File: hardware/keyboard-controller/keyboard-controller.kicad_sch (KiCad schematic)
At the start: 35 parts, among them J1 Debug_Pins, SW1 MODE_SEL, SW2 SUB_MODE, SW3 CLK_DIV, U2 Pico, U3 MCP4921

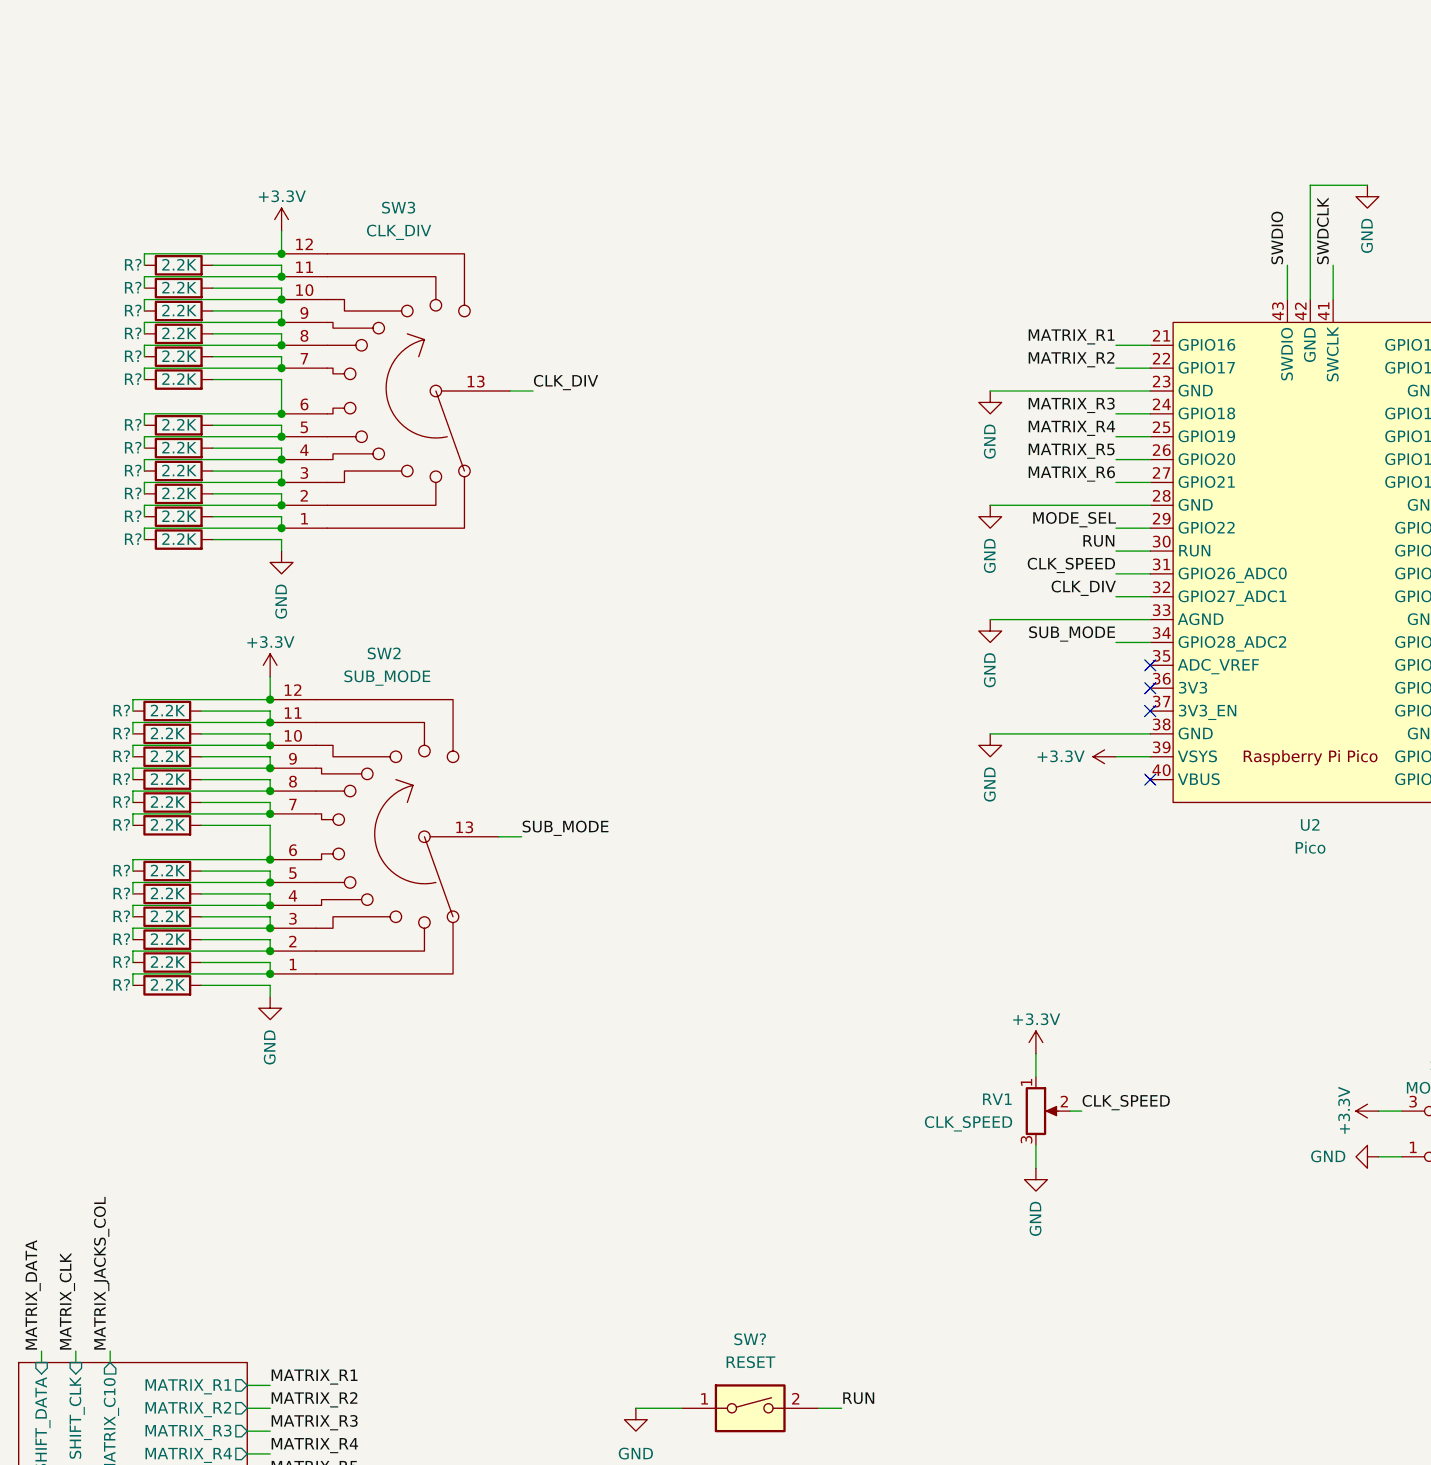
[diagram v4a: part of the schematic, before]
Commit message: Added filter caps on pots and rotary switches
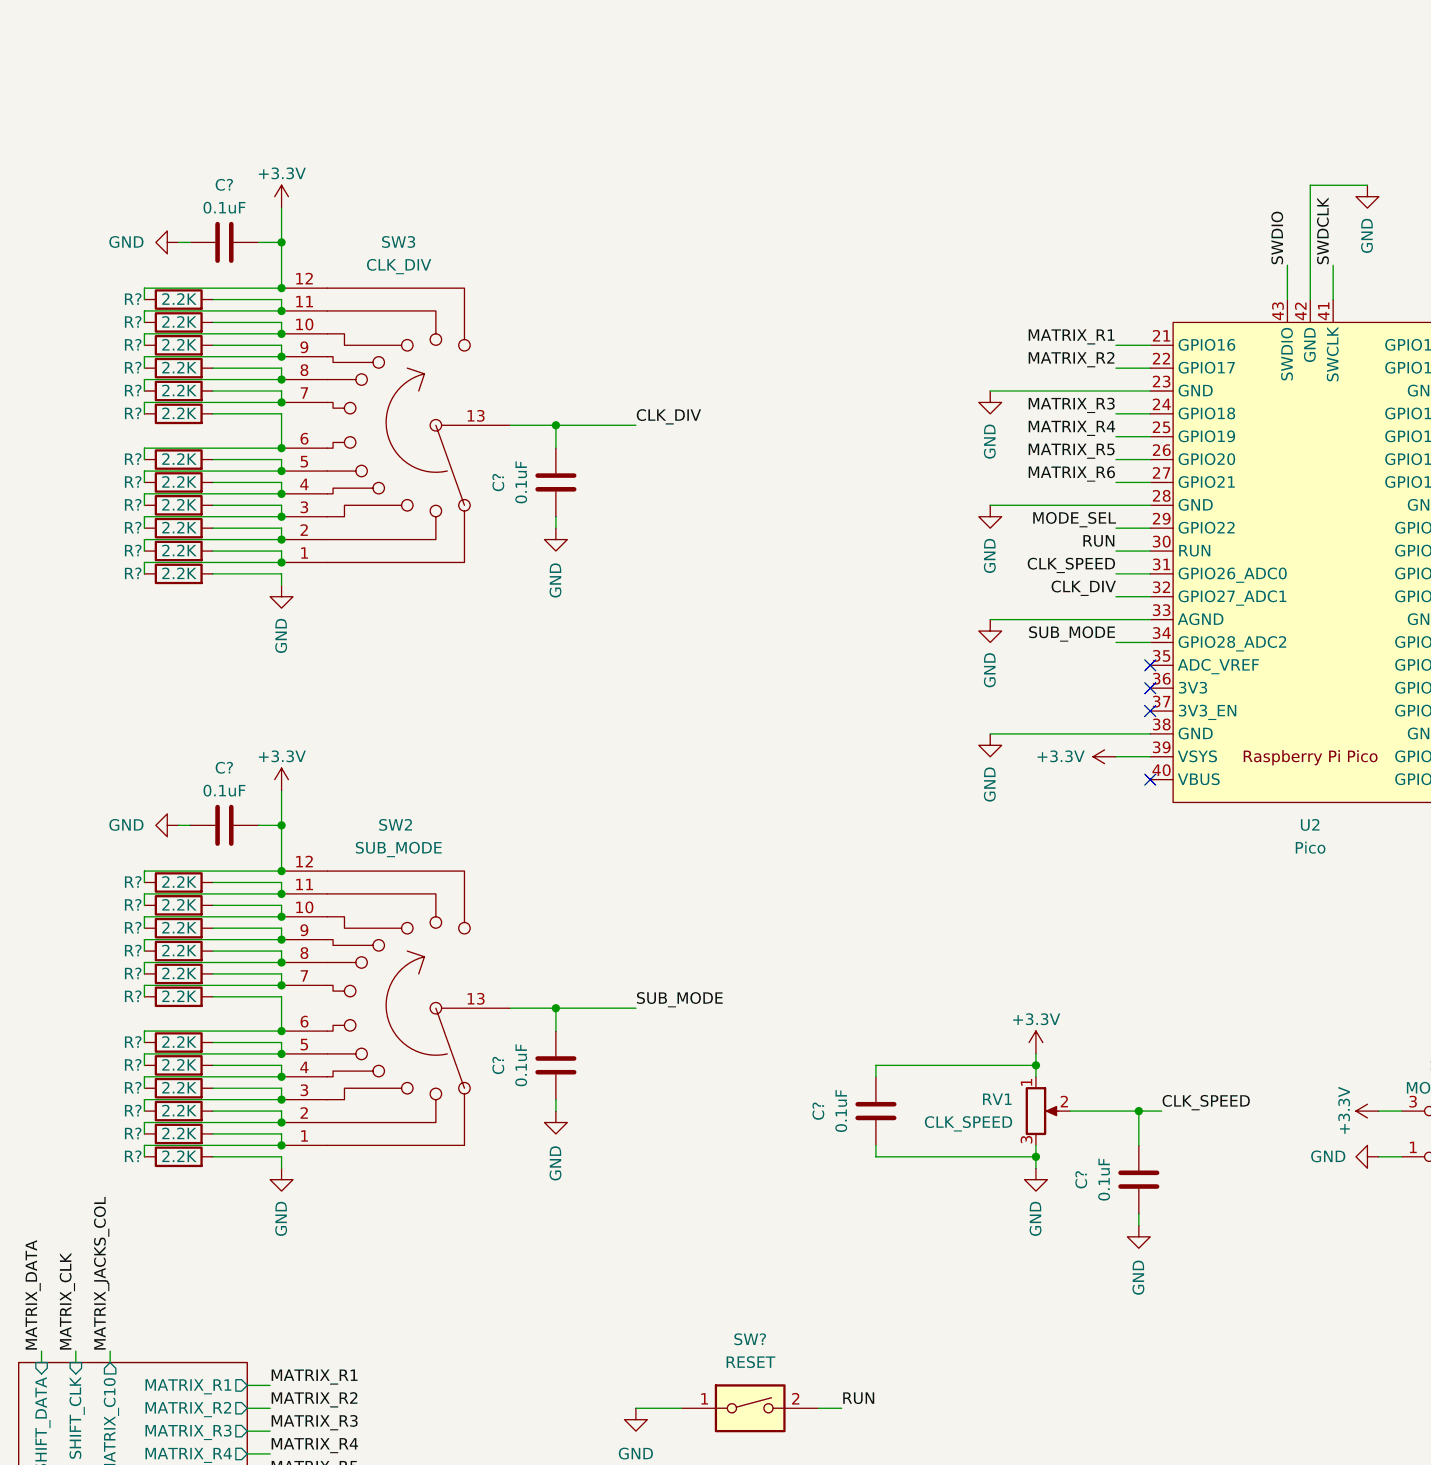
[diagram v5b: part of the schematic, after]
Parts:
- added C? (x6): 0.1uF, AEC_Capacitors:C_Disc_D5.0mm_W2.5mm_P3.0mm, symbol Device:C
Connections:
- net +3V3: now also C?.2, C?.2, C?.2
- net CLK_DIV: now also C?.2
- net CLK_SPEED: now also C?.2
- net GND: now also C?.1, C?.1, C?.1, C?.1, C?.1, C?.1
- net SUB_MODE: now also C?.2
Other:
- moved on the sheet: R?, SW2, SW3

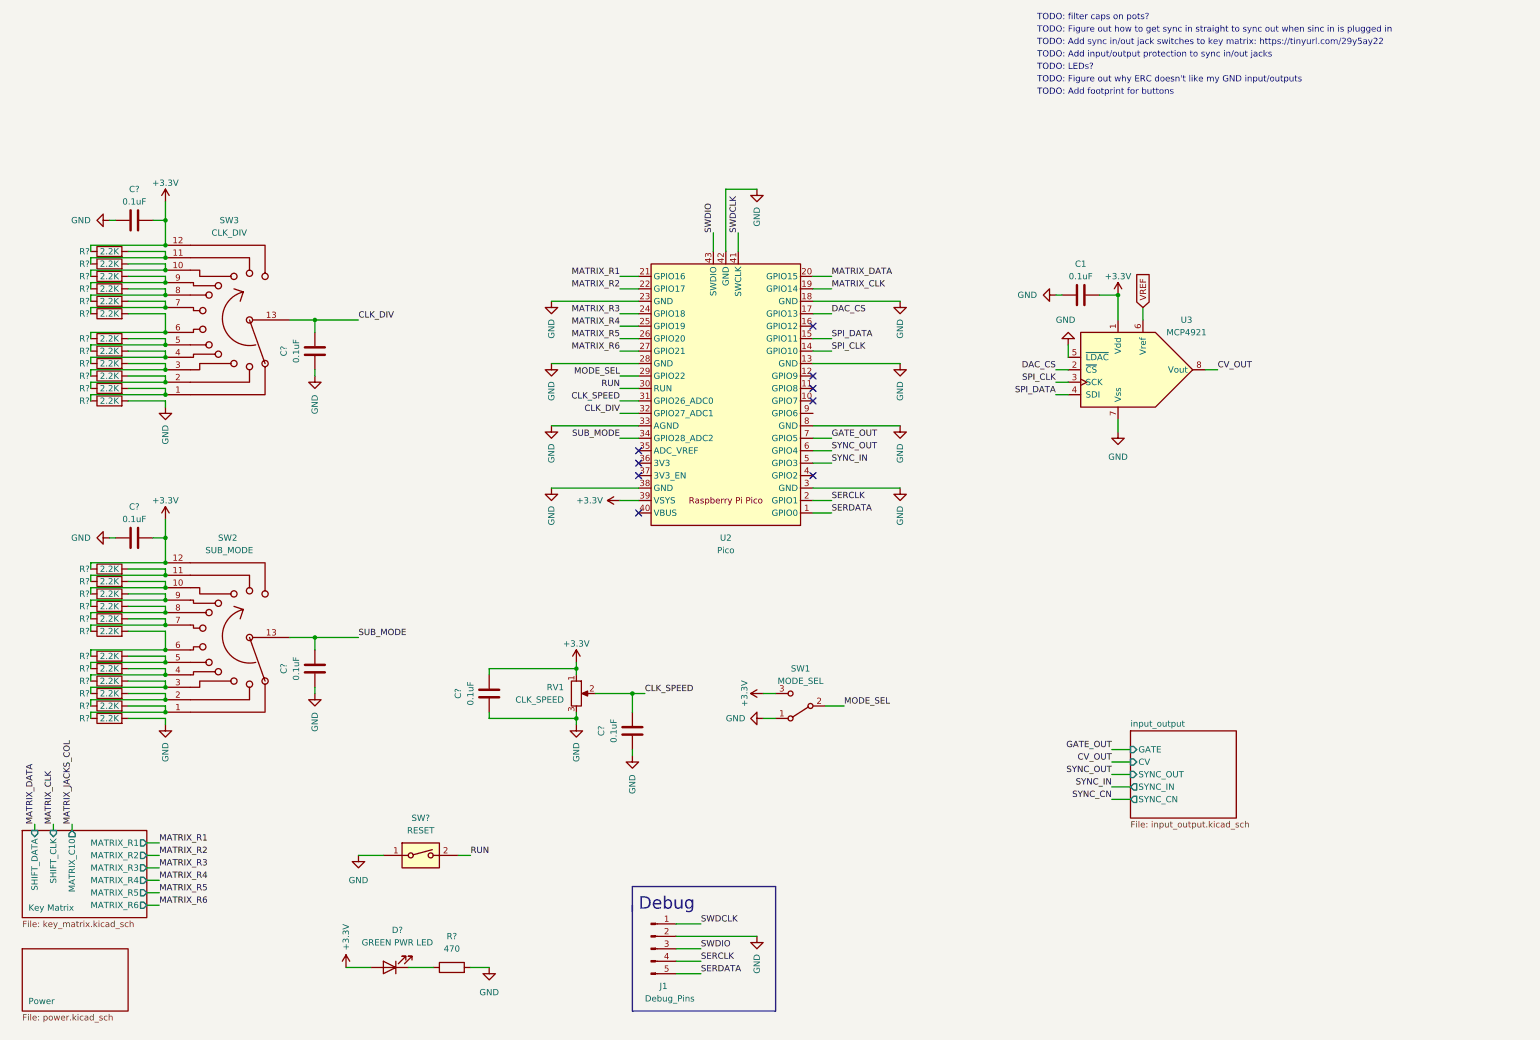
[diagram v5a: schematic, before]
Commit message: Added analog switch for analog input
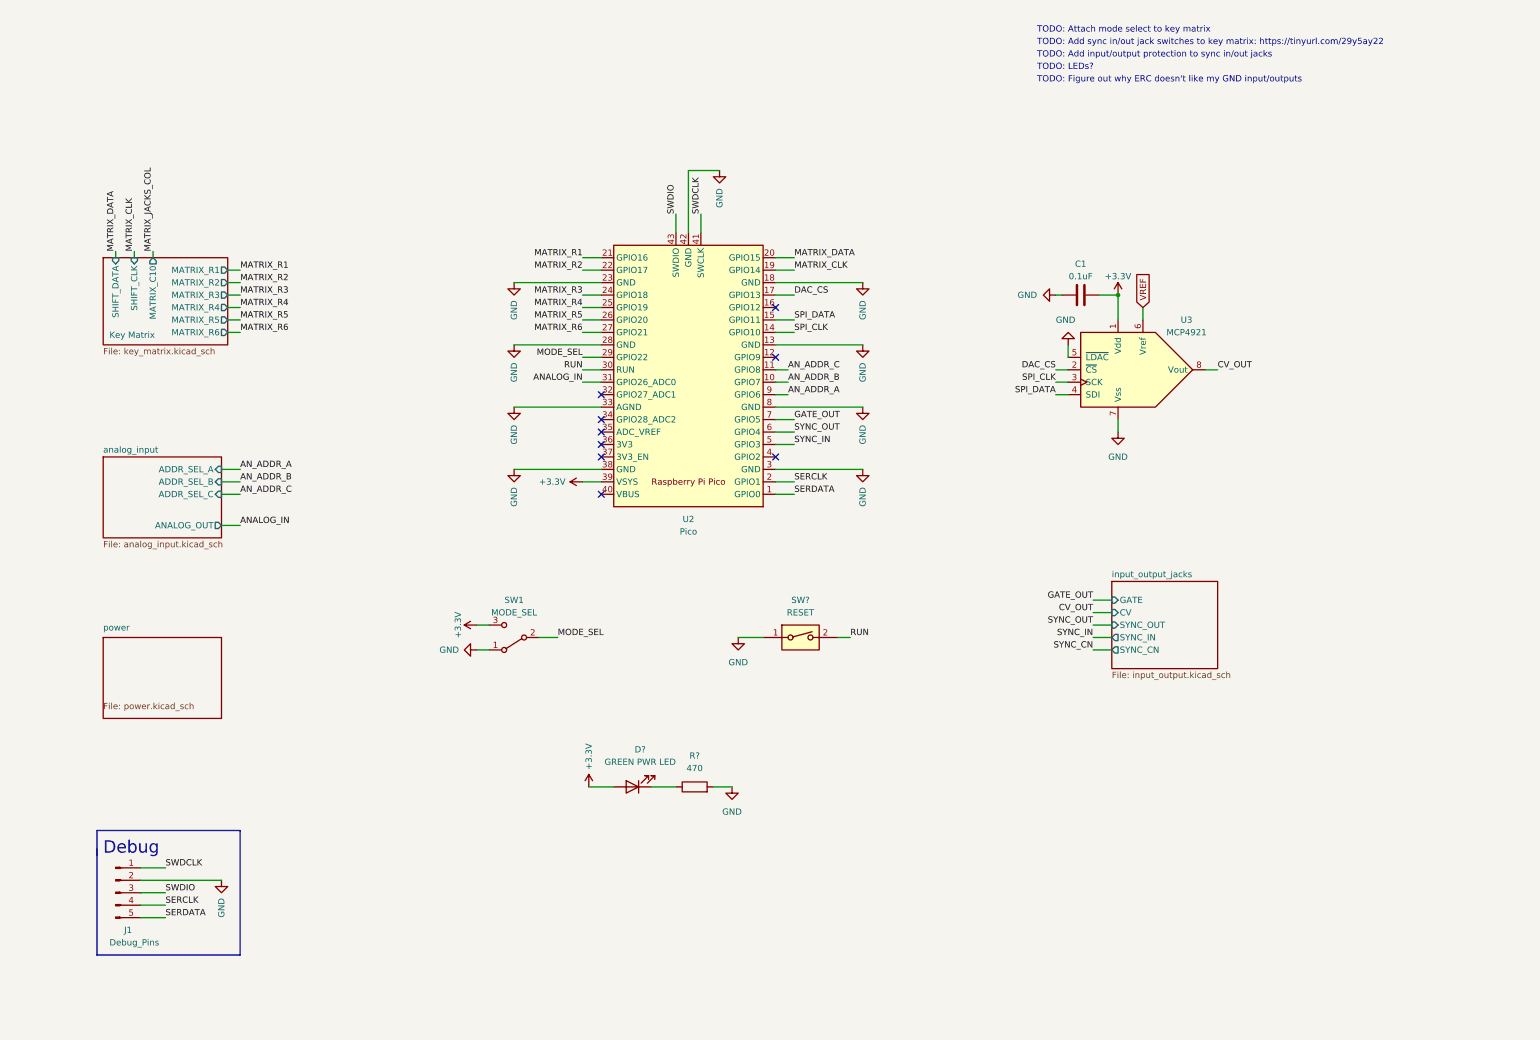
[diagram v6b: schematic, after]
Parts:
- removed C? (x6): 0.1uF, AEC_Capacitors:C_Disc_D5.0mm_W2.5mm_P3.0mm, symbol Device:C
- removed R? (x24): 2.2K, symbol Device:R
- removed RV1: CLK_SPEED, symbol Device:R_Potentiometer
- removed SW2: SUB_MODE, symbol Switch:SW_Rotary12
- removed SW3: CLK_DIV, symbol Switch:SW_Rotary12
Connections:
- net AN_ADDR_B: now reaches U2.10 (GPIO7)
- net AN_ADDR_C: now reaches U2.11 (GPIO8)
- net AN_ADDR_A: now reaches U2.9 (GPIO6)
- net CLK_DIV: no longer names the net of U2.32 (GPIO27_ADC1)
- net CLK_SPEED renamed ANALOG_IN
- net SUB_MODE: no longer names the net of U2.34 (GPIO28_ADC2)
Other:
- sheet Power renamed power
- sheet input_output renamed input_output_jacks
- added sheet analog_input (analog_input.kicad_sch)
- note added: "TODO: Attach mode select to key matrix"
- note removed: "TODO: Add footprint for buttons"
- note removed: "TODO: Figure out how to get sync in straight to sync out when sinc in is plugged in"
- note removed: "TODO: filter caps on pots?"
- moved on the sheet: D?, J1, R?, SW1, SW?, U2

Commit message: Added footprint for rotary switches
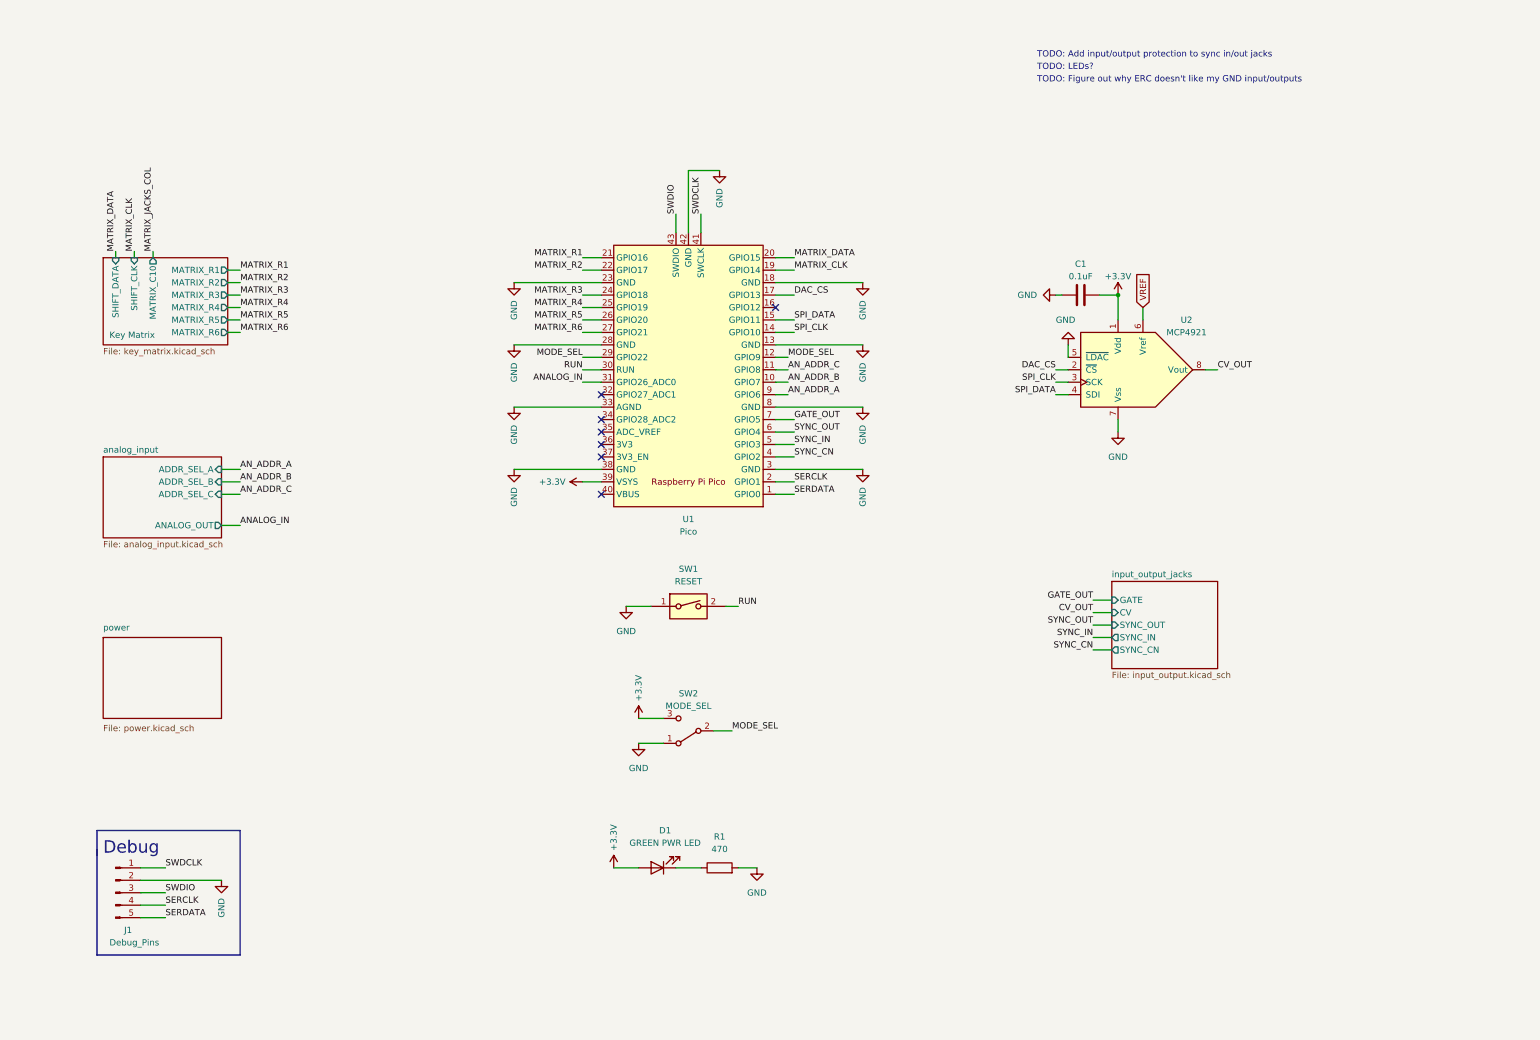
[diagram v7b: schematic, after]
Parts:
- removed SW1: MODE_SEL, symbol Switch:SW_SPDT
- added SW2: MODE_SEL, symbol Switch:SW_SPDT
- gave numbers to parts that had none: 3
- renumbered U2 to U1, U3 to U2
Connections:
- net +3V3: now also SW2.3 (C)
- net GND: now also SW2.1 (A)
- net MODE_SEL: now also U1.12 (GPIO9), SW2.2 (B)
- net SYNC_CN: now also U1.4 (GPIO2)
- no-connect marks 9 -> 7
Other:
- note removed: "TODO: Add sync in/out jack switches to key matrix: https://tinyurl.com/29y5ay22"
- note removed: "TODO: Attach mode select to key matrix"
- moved on the sheet: D1, R1, SW1
